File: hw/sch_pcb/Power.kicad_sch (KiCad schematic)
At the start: 20 parts

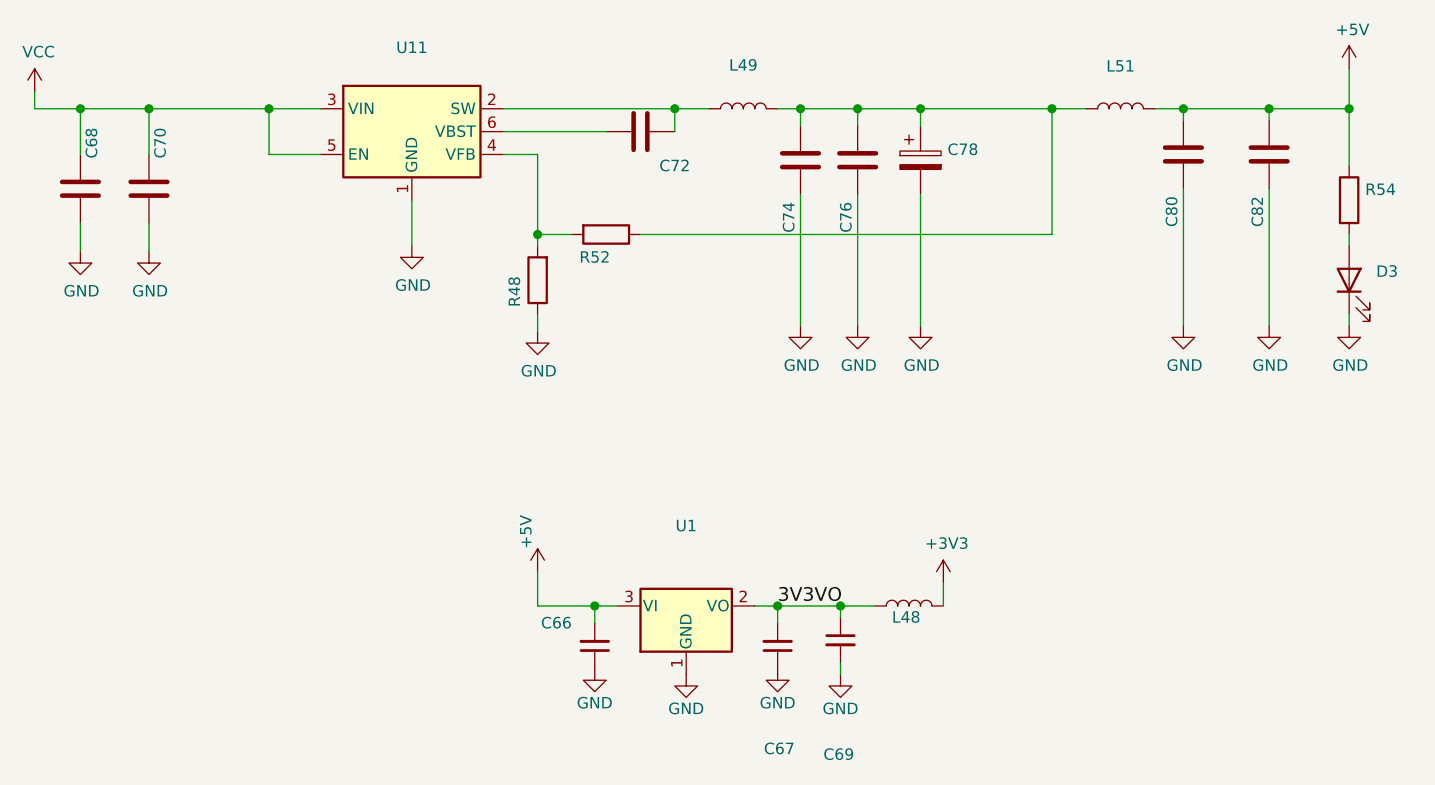
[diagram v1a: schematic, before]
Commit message: Add a link to clock buffer datasheet.
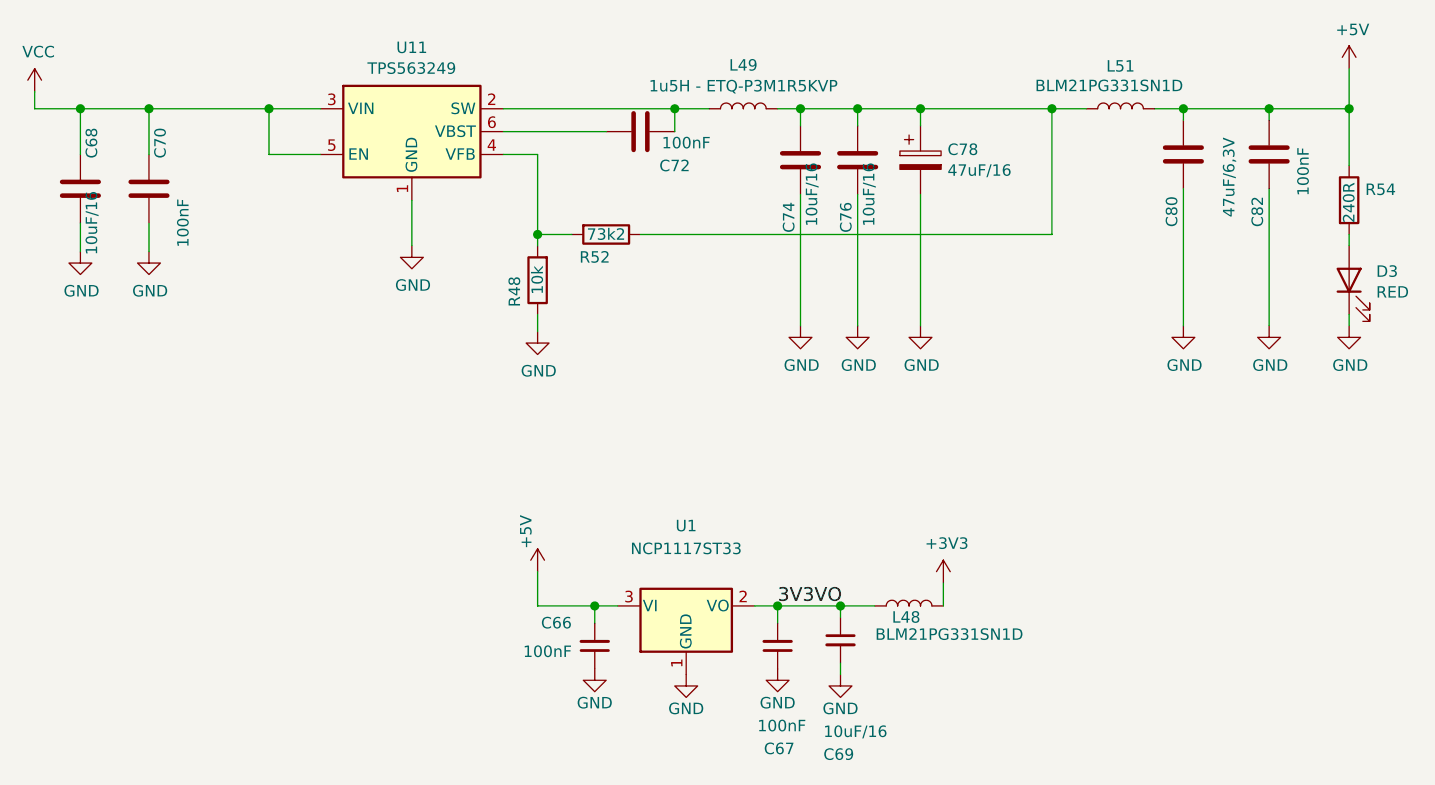
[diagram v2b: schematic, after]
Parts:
- C66, C67, C70, C72, C82: value (none) -> 100nF; footprint (none) -> Capacitor_SMD:C_0603_1608Metric
- C68, C69, C74, C76: value (none) -> 10uF/16; footprint (none) -> Capacitor_SMD:C_0805_2012Metric
- C78: value (none) -> 47uF/16; footprint (none) -> Mlab_C:TantalC_SizeC_Reflow
- C80: value (none) -> 47uF/6,3V; footprint (none) -> Capacitor_SMD:C_0805_2012Metric
- D3: value (none) -> RED; footprint (none) -> Mlab_D:LED_1206
- L48, L51: value (none) -> BLM21PG331SN1D; footprint (none) -> Inductor_SMD:L_0805_2012Metric_Pad1.15x1.40mm_HandSolder
- L49: value (none) -> 1u5H - ETQ-P3M1R5KVP; footprint (none) -> Mlab_L:PCC-M0530M-LP
- R48: value (none) -> 10k; footprint (none) -> Resistor_SMD:R_0603_1608Metric
- R52: value (none) -> 73k2; footprint (none) -> Resistor_SMD:R_0603_1608Metric
- R54: value (none) -> 240R; footprint (none) -> Resistor_SMD:R_0603_1608Metric
- U1: value (none) -> NCP1117ST33; footprint (none) -> Package_TO_SOT_SMD:SOT-223-3_TabPin2
- U11: value (none) -> TPS563249; footprint (none) -> Package_TO_SOT_SMD:SOT-23-6
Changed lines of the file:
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@@
     (in_bom yes) (on_board yes)
     (property "Reference" "C76" (id 0) (at 160.655 43.815 90))
-    (property "Value" "" (id 1) (at 163.195 41.275 90))
-    (property "Footprint" "" (id 2) (at 160.9598 33.655 0)
+    (property "Value" "10uF/16" (id 1) (at 163.195 41.275 90))
+    (property "Footprint" "Capacitor_SMD:C_0805_2012Metric" (id 2) (at 160.9598 33.655 0)
       (effects (font (size 1.27 1.27)) hide)
     )
@@
       (effects (font (size 1.27 1.27)) (justify left))
     )
-    (property "Value" "" (id 1) (at 130.175 92.075 0)
-      (effects (font (size 1.27 1.27)) (justify left))
-    )
-    (property "Footprint" "" (id 2) (at 132.715 91.44 0)
+    (property "Value" "100nF" (id 1) (at 130.175 92.075 0)
+      (effects (font (size 1.27 1.27)) (justify left))
+    )
+    (property "Footprint" "Capacitor_SMD:C_0603_1608Metric" (id 2) (at 132.715 91.44 0)
       (effects (font (size 1.524 1.524)) hide)
     )
@@
     (in_bom yes) (on_board yes)
     (property "Reference" "C72" (id 0) (at 141.605 38.1 90))
-    (property "Value" "" (id 1) (at 142.875 35.56 90))
-    (property "Footprint" "" (id 2) (at 133.985 35.2552 0)
+    (property "Value" "100nF" (id 1) (at 142.875 35.56 90))
+    (property "Footprint" "Capacitor_SMD:C_0603_1608Metric" (id 2) (at 133.985 35.2552 0)
       (effects (font (size 1.27 1.27)) hide)
     )
@@
     (in_bom yes) (on_board yes)
     (property "Reference" "L51" (id 0) (at 191.135 27.0318 90))
-    (property "Value" "" (id 1) (at 189.865 29.21 90))
-    (property "Footprint" "" (id 2) (at 191.135 31.75 0)
+    (property "Value" "BLM21PG331SN1D" (id 1) (at 189.865 29.21 90))
+    (property "Footprint" "Inductor_SMD:L_0805_2012Metric_Pad1.15x1.40mm_HandSolder" (id 2) (at 191.135 31.75 0)
       (effects (font (size 1.27 1.27)) hide)
     )
@@
     (in_bom yes) (on_board yes)
     (property "Reference" "C80" (id 0) (at 196.85 43.18 90))
-    (property "Value" "" (id 1) (at 203.2 39.37 90))
-    (property "Footprint" "" (id 2) (at 197.1548 33.02 0)
+    (property "Value" "47uF/6,3V" (id 1) (at 203.2 39.37 90))
+    (property "Footprint" "Capacitor_SMD:C_0805_2012Metric" (id 2) (at 197.1548 33.02 0)
       (effects (font (size 1.27 1.27)) hide)
     )
@@
       (effects (font (size 1.27 1.27)) (justify left))
     )
-    (property "Value" "" (id 1) (at 171.9072 38.608 0)
-      (effects (font (size 1.27 1.27)) (justify left))
-    )
-    (property "Footprint" "" (id 2) (at 169.8752 41.275 0)
+    (property "Value" "47uF/16" (id 1) (at 171.9072 38.608 0)
+      (effects (font (size 1.27 1.27)) (justify left))
+    )
+    (property "Footprint" "Mlab_C:TantalC_SizeC_Reflow" (id 2) (at 169.8752 41.275 0)
       (effects (font (size 1.27 1.27)) hide)
     )
@@
       (effects (font (size 1.27 1.27)) (justify left))
     )
-    (property "Value" "" (id 1) (at 158.115 100.965 0)
-      (effects (font (size 1.27 1.27)) (justify left))
-    )
-    (property "Footprint" "" (id 2) (at 160.02 90.805 0)
+    (property "Value" "10uF/16" (id 1) (at 158.115 100.965 0)
+      (effects (font (size 1.27 1.27)) (justify left))
+    )
+    (property "Footprint" "Capacitor_SMD:C_0805_2012Metric" (id 2) (at 160.02 90.805 0)
       (effects (font (size 1.524 1.524)) hide)
     )
@@
     (in_bom yes) (on_board yes)
     (property "Reference" "L49" (id 0) (at 149.225 26.924 90))
-    (property "Value" "" (id 1) (at 149.225 29.2354 90))
-    (property "Footprint" "" (id 2) (at 149.225 31.75 0)
+    (property "Value" "1u5H - ETQ-P3M1R5KVP" (id 1) (at 149.225 29.2354 90))
+    (property "Footprint" "Mlab_L:PCC-M0530M-LP" (id 2) (at 149.225 31.75 0)
       (effects (font (size 1.27 1.27)) hide)
     )
@@
       (effects (font (size 1.27 1.27)) (justify left))
     )
-    (property "Value" "" (id 1) (at 180.34 90.17 90)
-      (effects (font (size 1.27 1.27)) (justify left))
-    )
-    (property "Footprint" "" (id 2) (at 167.64 86.995 0)
+    (property "Value" "BLM21PG331SN1D" (id 1) (at 180.34 90.17 90)
+      (effects (font (size 1.27 1.27)) (justify left))
+    )
+    (property "Footprint" "Inductor_SMD:L_0805_2012Metric_Pad1.15x1.40mm_HandSolder" (id 2) (at 167.64 86.995 0)
       (effects (font (size 1.27 1.27)) hide)
     )
@@
     (in_bom yes) (on_board yes)
     (property "Reference" "R52" (id 0) (at 132.715 48.26 90))
-    (property "Value" "" (id 1) (at 133.985 45.72 90))
-    (property "Footprint" "" (id 2) (at 133.985 43.942 90)
+    (property "Value" "73k2" (id 1) (at 133.985 45.72 90))
+    (property "Footprint" "Resistor_SMD:R_0603_1608Metric" (id 2) (at 133.985 43.942 90)
       (effects (font (size 1.27 1.27)) hide)
     )
@@
     (in_bom yes) (on_board yes)
     (property "Reference" "C74" (id 0) (at 154.305 43.815 90))
-    (property "Value" "" (id 1) (at 156.845 41.275 90))
-    (property "Footprint" "" (id 2) (at 154.6098 33.655 0)
+    (property "Value" "10uF/16" (id 1) (at 156.845 41.275 90))
+    (property "Footprint" "Capacitor_SMD:C_0805_2012Metric" (id 2) (at 154.6098 33.655 0)
       (effects (font (size 1.27 1.27)) hide)
     )
@@
     (in_bom yes) (on_board yes)
     (property "Reference" "U11" (id 0) (at 112.395 24.9682 0))
-    (property "Value" "" (id 1) (at 112.395 27.2796 0))
-    (property "Footprint" "" (id 2) (at 113.665 40.64 0)
+    (property "Value" "TPS563249" (id 1) (at 112.395 27.2796 0))
+    (property "Footprint" "Package_TO_SOT_SMD:SOT-23-6" (id 2) (at 113.665 40.64 0)
       (effects (font (size 1.27 1.27)) (justify left) hide)
     )
@@
       (effects (font (size 1.27 1.27)) (justify right))
     )
-    (property "Value" "" (id 1) (at 219.5322 52.1462 90)
+    (property "Value" "RED" (id 1) (at 219.5322 52.1462 90)
       (effects (font (size 1.27 1.27)) (justify right))
     )
-    (property "Footprint" "" (id 2) (at 216.535 50.8 0)
+    (property "Footprint" "Mlab_D:LED_1206" (id 2) (at 216.535 50.8 0)
       (effects (font (size 1.27 1.27)) hide)
     )
@@
     (in_bom yes) (on_board yes)
     (property "Reference" "U1" (id 0) (at 142.875 78.105 0))
-    (property "Value" "" (id 1) (at 142.875 80.645 0))
-    (property "Footprint" "" (id 2) (at 142.875 81.915 0)
+    (property "Value" "NCP1117ST33" (id 1) (at 142.875 80.645 0))
+    (property "Footprint" "Package_TO_SOT_SMD:SOT-223-3_TabPin2" (id 2) (at 142.875 81.915 0)
       (effects (font (size 1.27 1.27)) hide)
     )
@@
       (effects (font (size 1.27 1.27)) (justify left))
     )
-    (property "Value" "" (id 1) (at 156.21 100.33 0)
-      (effects (font (size 1.27 1.27)) (justify left))
-    )
-    (property "Footprint" "" (id 2) (at 153.035 91.44 0)
+    (property "Value" "100nF" (id 1) (at 156.21 100.33 0)
+      (effects (font (size 1.27 1.27)) (justify left))
+    )
+    (property "Footprint" "Capacitor_SMD:C_0603_1608Metric" (id 2) (at 153.035 91.44 0)
       (effects (font (size 1.524 1.524)) hide)
     )
@@
     (in_bom yes) (on_board yes)
     (property "Reference" "C70" (id 0) (at 84.455 35.56 90))
-    (property "Value" "" (id 1) (at 86.995 44.45 90))
-    (property "Footprint" "" (id 2) (at 82.2198 36.83 0)
+    (property "Value" "100nF" (id 1) (at 86.995 44.45 90))
+    (property "Footprint" "Capacitor_SMD:C_0603_1608Metric" (id 2) (at 82.2198 36.83 0)
       (effects (font (size 1.27 1.27)) hide)
     )
@@
     (in_bom yes) (on_board yes)
     (property "Reference" "C68" (id 0) (at 76.835 35.56 90))
-    (property "Value" "" (id 1) (at 76.835 44.45 90))
-    (property "Footprint" "" (id 2) (at 74.5998 36.83 0)
+    (property "Value" "10uF/16" (id 1) (at 76.835 44.45 90))
+    (property "Footprint" "Capacitor_SMD:C_0805_2012Metric" (id 2) (at 74.5998 36.83 0)
       (effects (font (size 1.27 1.27)) hide)
     )
@@
     (in_bom yes) (on_board yes)
     (property "Reference" "R48" (id 0) (at 123.825 52.07 90))
-    (property "Value" "" (id 1) (at 126.365 50.8 90))
-    (property "Footprint" "" (id 2) (at 128.143 50.8 90)
+    (property "Value" "10k" (id 1) (at 126.365 50.8 90))
+    (property "Footprint" "Resistor_SMD:R_0603_1608Metric" (id 2) (at 128.143 50.8 90)
       (effects (font (size 1.27 1.27)) hide)
     )
@@
       (effects (font (size 1.27 1.27)) (justify left))
     )
-    (property "Value" "" (id 1) (at 216.535 44.45 90)
-      (effects (font (size 1.27 1.27)) (justify left))
-    )
-    (property "Footprint" "" (id 2) (at 214.757 41.91 90)
+    (property "Value" "240R" (id 1) (at 216.535 44.45 90)
+      (effects (font (size 1.27 1.27)) (justify left))
+    )
+    (property "Footprint" "Resistor_SMD:R_0603_1608Metric" (id 2) (at 214.757 41.91 90)
       (effects (font (size 1.27 1.27)) hide)
     )
@@
     (in_bom yes) (on_board yes)
     (property "Reference" "C82" (id 0) (at 206.375 43.18 90))
-    (property "Value" "" (id 1) (at 211.455 38.735 90))
-    (property "Footprint" "" (id 2) (at 206.6798 33.02 0)
-      (effects (font (size 1.27 1.27)) hide)
-    )
+    (property "Value" "100nF" (id 1) (at 211.455 38.735 90))
+    (property "Footprint" "Capacitor_SMD:C_0603_1608Metric" (id 2) (at 206.6798 33.02 0)
+      (effects (font (size 1.27 1.27)) hide)
+    )
